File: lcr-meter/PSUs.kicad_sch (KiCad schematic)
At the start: 32 parts, among them J19 Barrel_Jack, Q1 DMP3013SFV-7, U16 AP64501SP-13

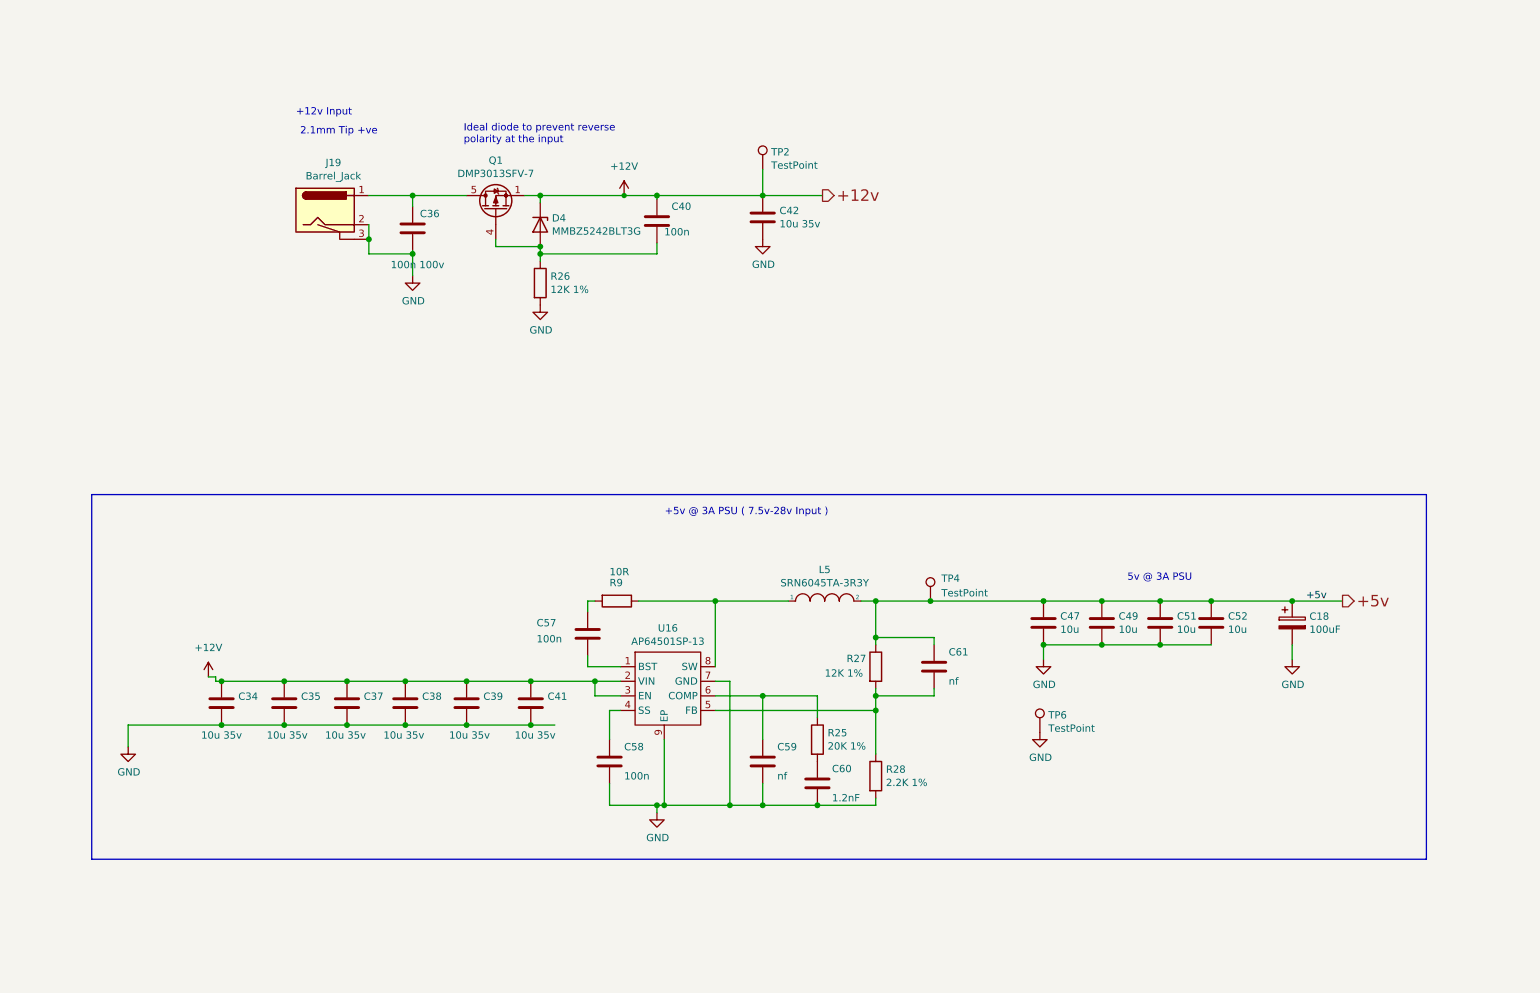
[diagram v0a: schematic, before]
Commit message: Schematic updates, added -5V, finalized sensing
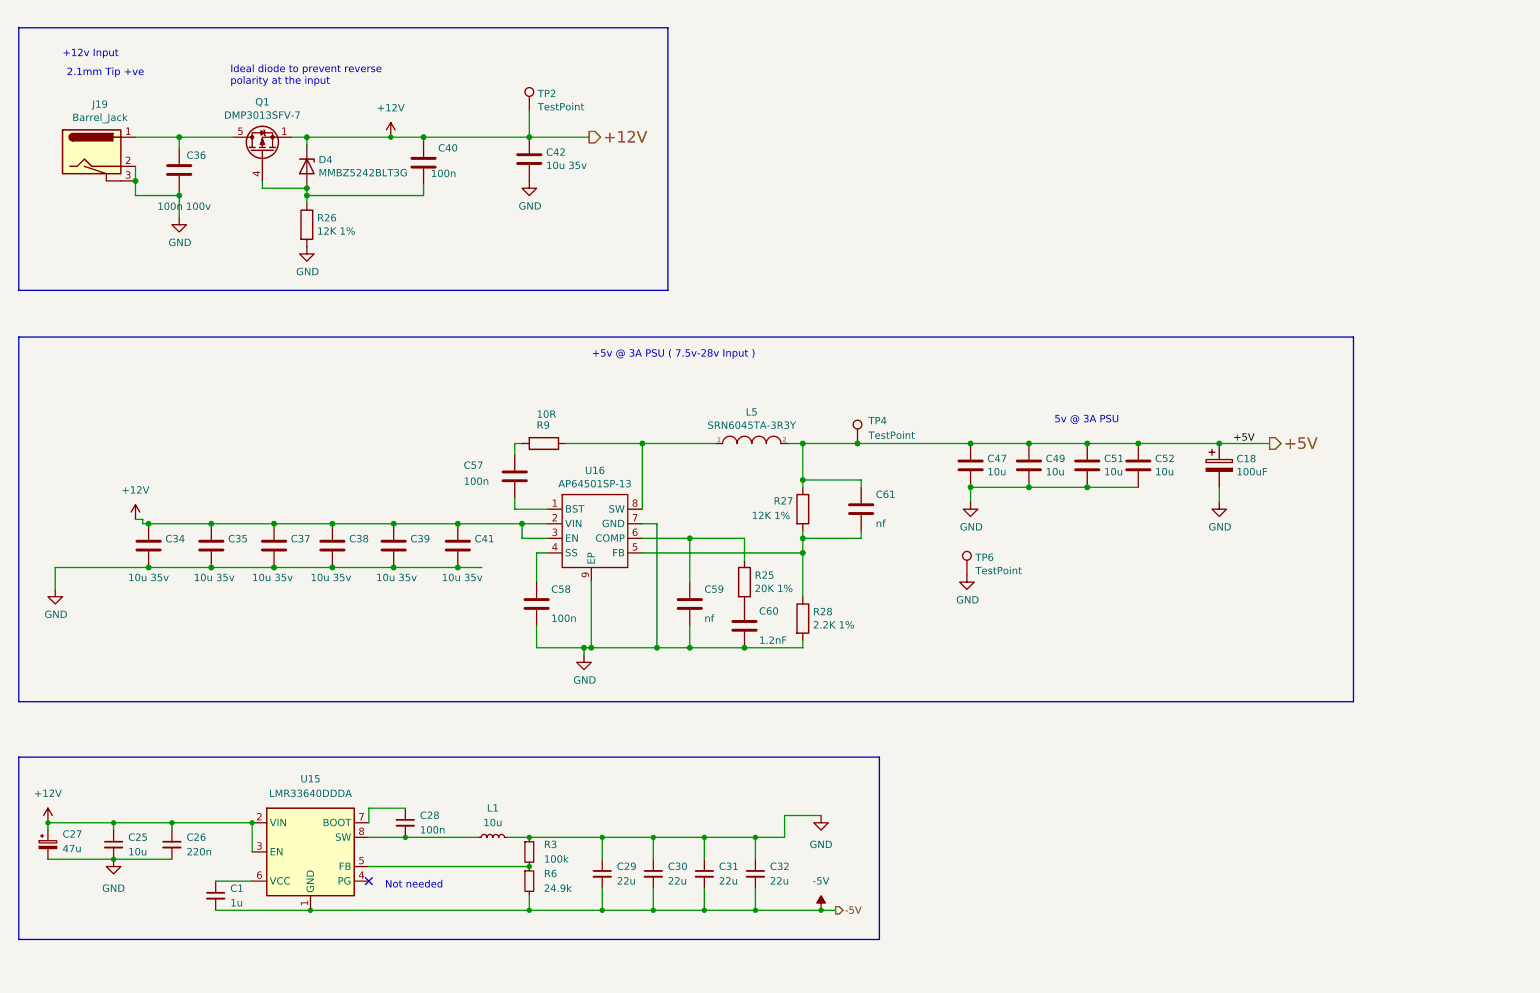
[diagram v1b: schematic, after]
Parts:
- added C1: 1u, symbol Device:C_Small
- added C25: 10u, symbol Device:C_Small
- added C26: 220n, symbol Device:C_Small
- added C27: 47u, symbol Device:C_Polarized_Small
- added C28: 100n, symbol Device:C_Small
- added C29, C30, C31, C32: 22u, symbol Device:C_Small
- added L1: 10u, symbol Device:L_Small
- added R3: 100k, symbol Device:R_Small
- added R6: 24.9k, symbol Device:R_Small
- added U15: LMR33640DDDA, Package_SO:Texas_HSOP-8-1EP_3.9x4.9mm_P1.27mm_ThermalVias, symbol Regulator_Switching:LMR33640DDDA
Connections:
- net +12V: now also C25.1, C26.1, C27.1, U15.2 (VIN), U15.3 (EN)
- net GND: now also C25.2, C26.2, C27.2, C29.1, C30.1, C31.1, C32.1, L1.2, R3.1
- net +5v renamed +5V
- new net: R3.2, R6.1, U15.5 (FB)
- new net: C1.1, U15.6 (VCC)
- new net: C28.1, U15.7 (BOOT)
- new net: C28.2, L1.1, U15.8 (SW)
- new net -5V: C1.2, C29.2, C30.2, C31.2, C32.2, R6.2, U15.1 (GND), U15.9 (GND)
- no-connect marks 0 -> 1
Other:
- note added: "Not needed"
- moved on the sheet: C18, C34, C35, C36, C37, C38, C39, C40, C41, C42, C47, C49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

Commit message: Addressable LED test board
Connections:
- net +12V: now also D4.3 (K); no longer D4.1 (K)
- net at C40.2, Q1.4 (G), R26.1: now also D4.1 (A); no longer D4.2 (A)

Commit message: Schematic completion
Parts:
- added C10, C11, C8, C9: 10u, symbol Device:C_Small
- added R11, R14: 1k, symbol Device:R_Small
- added R12: 1.6k, symbol Device:R_Small
- added R13: 500R, symbol Device:R_Small
- added U6, U7: LM1117MP-ADJ, Package_TO_SOT_SMD:SOT-223-3_TabPin2, symbol Regulator_Linear:LM1117MP-ADJ
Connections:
- net +5V: now also C10.1, C8.1, U6.3 (VI), U7.3 (VI)
- net GND: now also C10.2, C11.2, C8.2, C9.2, R12.2, R13.2
- new net: R13.1, R14.2, U7.1 (ADJ)
- new net: R11.2, R12.1, U6.1 (ADJ)
- new net +1V8: C11.1, R14.1, U7.2 (VO)
- new net +3V3: C9.1, R11.1, U6.2 (VO)
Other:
- note added: "1V8 Linear Regulation"
- note added: "3V3 Linear Regulation"
- note added: "V_out = 1.25V * (1 + R12 / R11) V_out = 3.25 V"
- note added: "V_out = 1.25V * (1 + R13 / R14) V_out = 1.875 V"

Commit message: Schematic polishing
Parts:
- removed C18: 100uF, Capacitor_Tantalum_SMD:CP_EIA-7343-31_Kemet-D, symbol Device:CP
- removed C34, C35, C37, C38, C39, C41: 10u 35v, Capacitor_SMD:C_0805_2012Metric, symbol Device:C
- removed C36: 100n 100v, Capacitor_SMD:C_0402_1005Metric, symbol Device:C
- removed C47, C49, C51, C52: 10u, Capacitor_SMD:C_0805_2012Metric, symbol Device:C
- removed C57, C58: 100n, Capacitor_SMD:C_0402_1005Metric, symbol Device:C
- removed C59, C61: nf, Capacitor_SMD:C_0402_1005Metric, symbol Device:C
- removed C60: 1.2nF, Capacitor_SMD:C_0402_1005Metric, symbol Device:C
- removed L5: SRN6045TA-3R3Y, Inductor_SMD:L_Bourns_SRN6045TA, symbol pspice:INDUCTOR
- removed R25: 20K 1%, Resistor_SMD:R_0402_1005Metric, symbol Device:R
- removed R27: 12K 1%, Resistor_SMD:R_0402_1005Metric, symbol Device:R
- removed R28: 2.2K 1%, Resistor_SMD:R_0402_1005Metric, symbol Device:R
- removed R9: 10R, Resistor_SMD:R_0402_1005Metric, symbol Device:R
- removed TP4, TP6: TestPoint, TestPoint:TestPoint_Pad_2.0x2.0mm, symbol Connector:TestPoint
- removed U16: AP64501SP-13, Package_SO:SOIC-8-1EP_3.9x4.9mm_P1.27mm_EP2.95x4.9mm_Mask2.71x3.4mm_ThermalVias, symbol CM4IO:AP64351
- added C18: 47u, Capacitor_SMD:CP_Elec_6.3x7.7, symbol Device:C_Polarized_Small
- added C34: 10u, Capacitor_SMD:C_0805_2012Metric, symbol Device:C_Small
- added C35: 220n, Capacitor_SMD:C_0805_2012Metric, symbol Device:C_Small
- added C37: 1u, Capacitor_SMD:C_0402_1005Metric, symbol Device:C_Small
- added C38: 100n, Capacitor_SMD:C_0805_2012Metric, symbol Device:C_Small
- added C39, C41, C47, C49: 22u, Capacitor_SMD:C_0805_2012Metric, symbol Device:C_Small
- added L2: 3.3u, footprints:IND_223NLT_PUL, symbol Device:L_Small
- added R19, R20, R21, R23: 0R, Resistor_SMD:R_0402_1005Metric, symbol Device:R_Small
- added R2: 100k, Resistor_SMD:R_0402_1005Metric, symbol Device:R_Small
- added R9: 24.9k, Resistor_SMD:R_0402_1005Metric, symbol Device:R_Small
- added U13: LMR33640DDDA, Package_SO:Texas_HSOP-8-1EP_3.9x4.9mm_P1.27mm_ThermalVias, symbol Regulator_Switching:LMR33640DDDA
- C1, C10, C11, C26, C28, C8, C9: footprint (none) -> Capacitor_SMD:C_0402_1005Metric
- C25, C29, C30, C31, C32: footprint (none) -> Capacitor_SMD:C_0805_2012Metric
- C27: footprint (none) -> Capacitor_SMD:CP_Elec_6.3x7.7; PN (none) -> EEE-HC1E470XP
- C42: value 10u 35v -> 10u
- D4: footprint Diode_SMD:D_SOT-23_ANK -> Package_TO_SOT_SMD:SOT-23
- J19: footprint CM4IO:BarrelJack_Horizontal -> Connector_BarrelJack:BarrelJack_Horizontal
- L1: value 10u -> 3.3u; footprint (none) -> footprints:IND_223NLT_PUL; PN (none) -> PA4340.332ANLT
- R11, R12, R13, R14, R3, R6: footprint (none) -> Resistor_SMD:R_0402_1005Metric
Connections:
- net +12V: now also C18.1, C34.1, C35.1, U13.2 (VIN), U13.3 (EN)
- net +1V8: now also R23.2; no longer C11.1, R14.1, U7.2 (VO)
- net +3V3: now also R21.2; no longer C9.1, R11.1, U6.2 (VO)
- net +5V: now also R19.2
- net -5V: now also R20.2; no longer C1.2, C29.2, C30.2, C31.2, C32.2, R6.2, U15.1 (GND), U15.9 (GND)
- net GND: now also C18.2, C34.2, C35.2, C37.2, C39.2, C41.2, C47.2, C49.2, R9.2, U13.1 (GND), U13.9 (GND)
- new net: C1.2, C29.2, C30.2, C31.2, C32.2, R20.1, R6.2, U15.1 (GND), U15.9 (GND)
- new net: C39.1, C41.1, C47.1, C49.1, L2.2, R19.1, R2.1
- new net: C11.1, R14.1, R23.1, U7.2 (VO)
- new net: C9.1, R11.1, R21.1, U6.2 (VO)
- new net: C38.2, L2.1, U13.8 (SW)
- new net: R2.2, R9.1, U13.5 (FB)
- new net: C37.1, U13.6 (VCC)
- new net: C38.1, U13.7 (BOOT)
- no-connect marks 1 -> 2
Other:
- note added: "ALL CAPS IN BOM MUST BE 35V RATED CAPS."
- note removed: "+5v @ 3A PSU ( 7.5v-28v Input )"
- note removed: "5v @ 3A PSU"
- moved on the sheet: C8, C9, J19, R11, R12, U6

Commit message: Component grouping started
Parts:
- removed TP2: TestPoint, TestPoint:TestPoint_Pad_2.0x2.0mm, symbol Connector:TestPoint
- C10, C11, C8, C9: footprint Capacitor_SMD:C_0402_1005Metric -> Capacitor_SMD:C_0805_2012Metric
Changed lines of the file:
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@@
 	(wire
 		(pts
-			(xy 107.95 30.988) (xy 107.95 35.56)
-		)
-		(stroke
-			(width 0)
-			(type solid)
-		)
-	)
-	(wire
-		(pts
 			(xy 157.48 170.18) (xy 158.75 170.18)
 		)
@@
 	)
 	(symbol
-		(lib_id "Connector:TestPoint")
-		(at 107.95 30.988 0)
-		(unit 1)
-		(exclude_from_sim no)
-		(in_bom yes)
-		(on_board yes)
-		(dnp no)
-		(property "Reference" "TP2"
-			(at 109.4232 27.9908 0)
-			(effects
-				(font
-					(size 1.27 1.27)
-				)
-				(justify left)
-			)
-		)
-		(property "Value" "TestPoint"
-			(at 109.4232 30.3022 0)
-			(effects
-				(font
-					(size 1.27 1.27)
-				)
-				(justify left)
-			)
-		)
-		(property "Footprint" "TestPoint:TestPoint_Pad_2.0x2.0mm"
-			(at 113.03 30.988 0)
-			(effects
-				(font
-					(size 1.27 1.27)
-				)
-				(hide yes)
-			)
-		)
-		(property "Datasheet" "~"
-			(at 113.03 30.988 0)
-			(effects
-				(font
-					(size 1.27 1.27)
-				)
-				(hide yes)
-			)
-		)
-		(property "Description" "test point"
-			(at 107.95 30.988 0)
-			(effects
-				(font
-					(size 1.27 1.27)
-				)
-				(hide yes)
-			)
-		)
-		(property "Field4" "nf"
-			(at 107.95 30.988 0)
-			(effects
-				(font
-					(size 1.27 1.27)
-				)
-				(hide yes)
-			)
-		)
-		(property "Field5" "nf"
-			(at 107.95 30.988 0)
-			(effects
-				(font
-					(size 1.27 1.27)
-				)
-				(hide yes)
-			)
-		)
-		(property "Field6" "nf"
-			(at 107.95 30.988 0)
-			(effects
-				(font
-					(size 1.27 1.27)
-				)
-				(hide yes)
-			)
-		)
-		(property "Field7" "nf"
-			(at 107.95 30.988 0)
-			(effects
-				(font
-					(size 1.27 1.27)
-				)
-				(hide yes)
-			)
-		)
-		(pin "1"
-		)
-		(instances
-			(project "lcr-meter"
-				(path "/ba333b18-b098-477b-9dd4-aab7b9764d9c/f2a8366c-faa8-47bd-8bfe-1b09106a7ae4"
-					(reference "TP2")
-					(unit 1)
-				)
-			)
-		)
-	)
-	(symbol
 		(lib_id "Transistor_FET:DMP3013SFV")
 		(at 61.468 38.1 90)
@@
 			)
 		)
-		(property "Footprint" "Capacitor_SMD:C_0402_1005Metric"
+		(property "Footprint" "Capacitor_SMD:C_0805_2012Metric"
 			(at 153.67 36.83 0)
 			(effects
@@
 			)
 		)
-		(property "Footprint" "Capacitor_SMD:C_0402_1005Metric"
+		(property "Footprint" "Capacitor_SMD:C_0805_2012Metric"
 			(at 254 36.83 0)
 			(effects
@@
 			)
 		)
-		(property "Footprint" "Capacitor_SMD:C_0402_1005Metric"
+		(property "Footprint" "Capacitor_SMD:C_0805_2012Metric"
 			(at 223.52 36.83 0)
 			(effects
@@
 			)
 		)
-		(property "Footprint" "Capacitor_SMD:C_0402_1005Metric"
+		(property "Footprint" "Capacitor_SMD:C_0805_2012Metric"
 			(at 184.15 36.83 0)
 			(effects

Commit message: Component grouping completed
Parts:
- C35, C38: footprint Capacitor_SMD:C_0805_2012Metric -> Capacitor_SMD:C_0402_1005Metric
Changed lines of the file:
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@@
 			)
 		)
-		(property "Footprint" "Capacitor_SMD:C_0805_2012Metric"
+		(property "Footprint" "Capacitor_SMD:C_0402_1005Metric"
 			(at 45.72 113.03 0)
 			(effects
@@
 			)
 		)
-		(property "Footprint" "Capacitor_SMD:C_0805_2012Metric"
+		(property "Footprint" "Capacitor_SMD:C_0402_1005Metric"
 			(at 86.36 109.22 0)
 			(effects

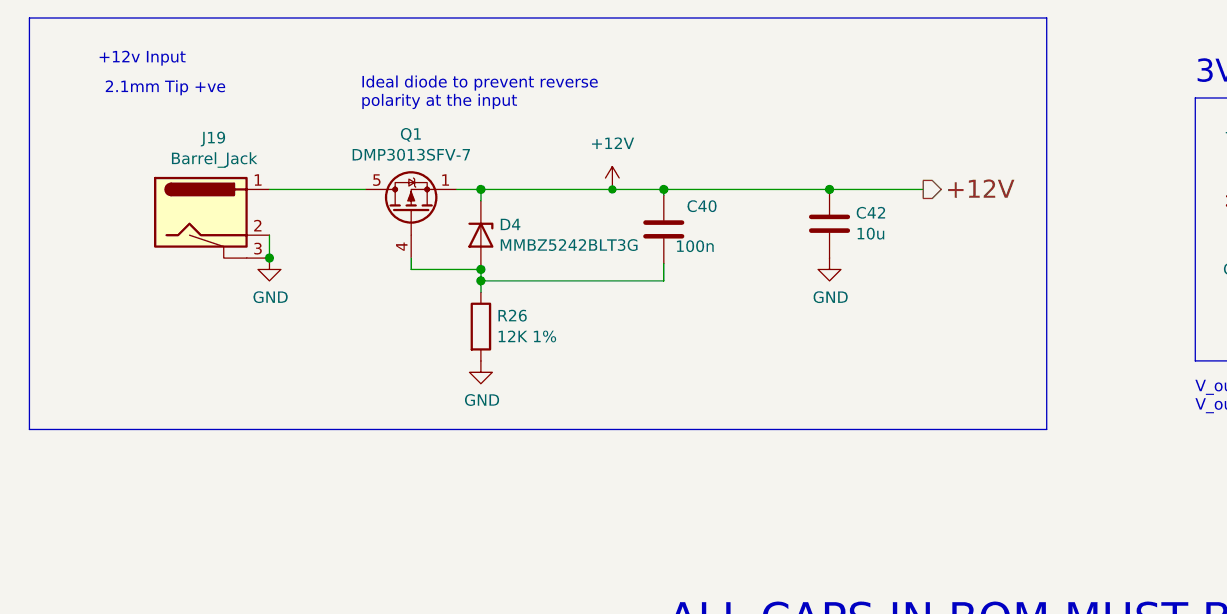
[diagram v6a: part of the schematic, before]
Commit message: Order submitteed, Mod board submitted
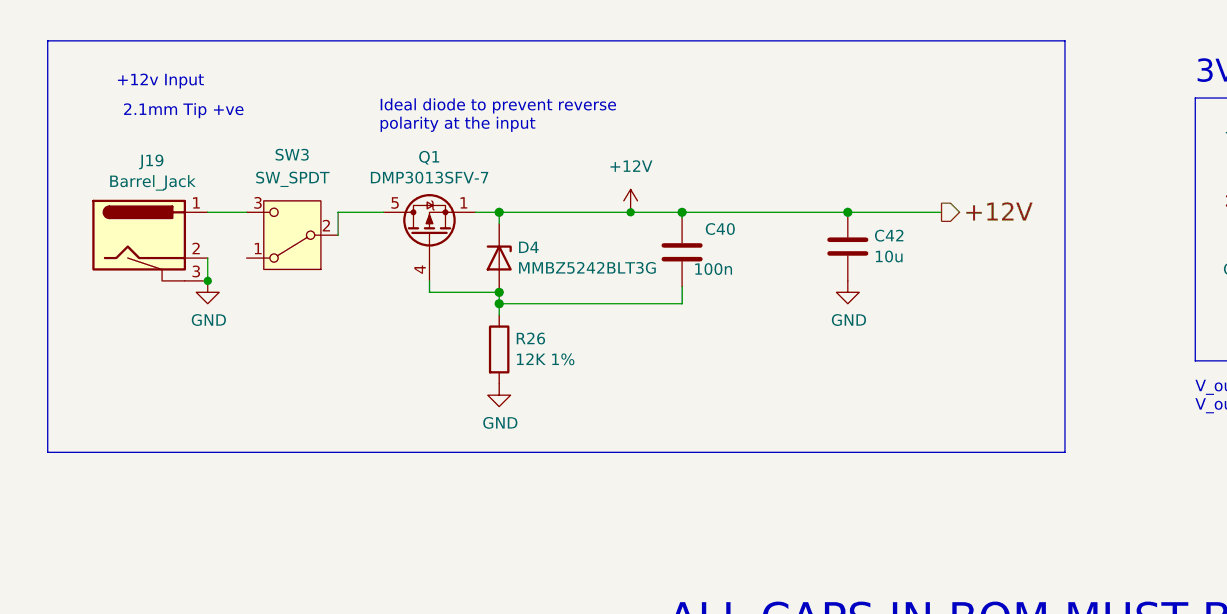
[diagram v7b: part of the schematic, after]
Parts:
- added SW3: SW_SPDT, Button_Switch_THT:SW_E-Switch_EG1224_SPDT_Angled, symbol Switch:SW_SPDT
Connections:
- net at J19.1: now also SW3.3 (C); no longer Q1.5 (D)
- new net: Q1.5 (D), SW3.2 (B)
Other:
- moved on the sheet: C40, C42, D4, J19, Q1, R26

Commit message: PCB updates
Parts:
- removed C10, C11: 10u, Capacitor_SMD:C_0805_2012Metric, symbol Device:C_Small
- removed J19: Barrel_Jack, Connector_BarrelJack:BarrelJack_Horizontal, symbol CM4IO:Barrel_Jack
- removed R13: 500R, Resistor_SMD:R_0402_1005Metric, symbol Device:R_Small
- removed R14: 1k, Resistor_SMD:R_0402_1005Metric, symbol Device:R_Small
- removed R19, R20, R21, R23: 0R, Resistor_SMD:R_0402_1005Metric, symbol Device:R_Small
- removed U7: LM1117MP-ADJ, Package_TO_SOT_SMD:SOT-223-3_TabPin2, symbol Regulator_Linear:LM1117MP-ADJ
- added J2: Conn_01x02, Connector_PinHeader_2.54mm:PinHeader_1x02_P2.54mm_Vertical, symbol Connector_Generic:Conn_01x02
- added JP1, JP2, JP3, JP4: Jumper_2_Open, Jumper:SolderJumper-2_P1.3mm_Open_TrianglePad1.0x1.5mm, symbol Jumper:Jumper_2_Open
- added R13, R14: 12k, Resistor_SMD:R_0402_1005Metric, symbol Device:R
- R26: value 12K 1% -> 12k
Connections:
- net +1V8: now also JP4.2 (B)
- net +3V3: now also JP3.2 (B)
- net +5V: now also JP1.2 (B)
- net -5V: now also JP2.2 (B)
- net GND: now also J2.2 (Pin_2), R14.2
- net at SW3.3 (C): now also J2.1 (Pin_1)
- net at C1.2, C29.2, C30.2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: now also JP2.1 (A)
- net at C39.1, C41.1, C47.1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: now also JP1.1 (A)
- net at C9.1, R11.1, U6.2 (VO): now also JP3.1 (A), R13.1
- new net: JP4.1 (A), R13.2, R14.1
- no-connect marks 2 -> 3
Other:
- note added: "+5V Buck"
- note added: "-5V Buck"
- note added: "Input Reverse Polarity Protection"
- note added: "Simpler 1V8 supply but will need some startup time"
- note removed: "1V8 Linear Regulation"
- note removed: "V_out = 1.25V * (1 + R13 / R14) V_out = 1.875 V"
- moved on the sheet: C1, C18, C25, C26, C27, C28, C29, C30, C31, C32, C34, C35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
